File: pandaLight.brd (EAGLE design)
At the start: 100 x 50 mm, 163 parts, among them J1 PJ-037A, U1 MIC23450AAAYML, U10 51, U11 TPD12S016PWR, U12 N25Q128AF8, U13 TPD12S016PWR, U14 AS4C128M16D3, U15 PMOD-2X6, U16 PMOD-2X6, U17 PLR135-T10, U18 PLT133-T10W, U19 PLR135-T10, U2 6SLX45CSG324, U20 TP10SQ, U21 TP10SQ, U22 PAN1322, U3 TPD4S014SON, U4 FT2232HL, U5 93LC46BT-I/OT, U6 51, U7 51, U8 TPD12S016PWR, U9 51, X1 USBUB-S, X2 HDMI_RECEPTICAL_A, X3 HDMI_RECEPTICAL_A, X4 HDMI_RECEPTICAL_A, Y1 403, Y2 20Mhz

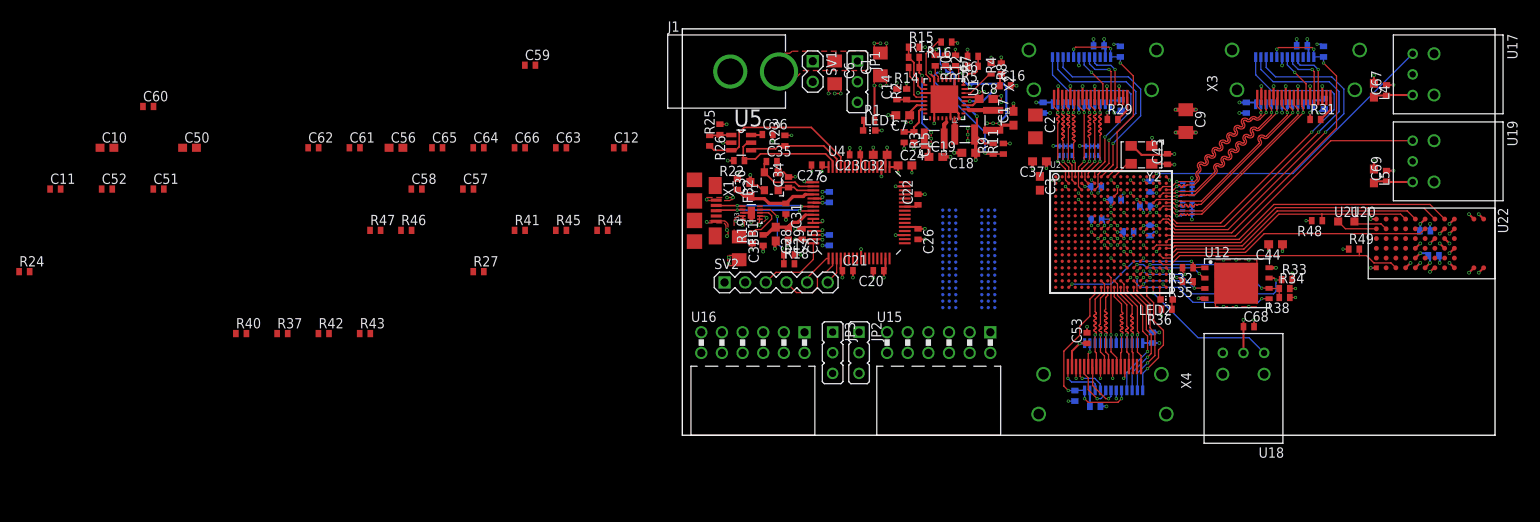
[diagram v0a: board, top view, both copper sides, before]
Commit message: Moved the pullup resistor networks and removed vias from the HDMI_RX* traces
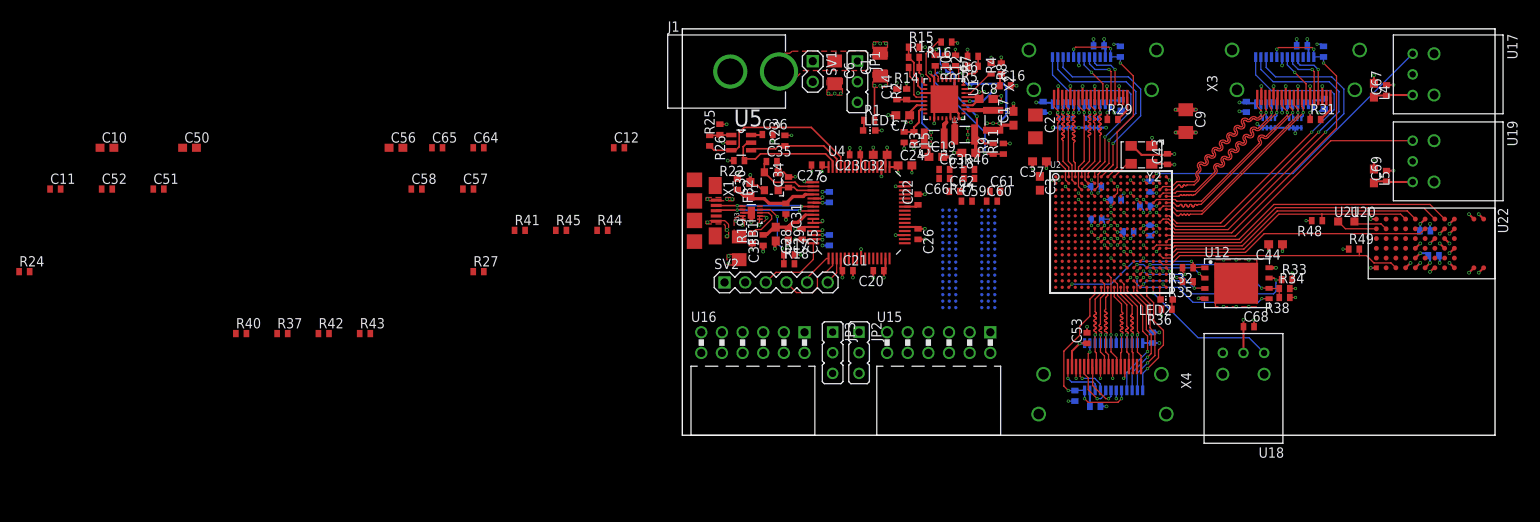
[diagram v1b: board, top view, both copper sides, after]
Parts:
- moved C60 104.5 mm to (38.1, 28.8)
- moved C62 79.1 mm to (33.5, 30.0)
- moved C61 79.0 mm to (38.5, 30.0)
- moved R47 73.3 mm to (35.3, 31.6), turned to 180 degrees
- moved R46 69.7 mm to (35.3, 32.7)
- moved C59 56.3 mm to (35.0, 28.8)
- moved C66 52.4 mm to (32.2, 31.6), turned to 180 degrees
- moved C63 47.2 mm to (32.2, 32.7)
- moved U10 16.9 mm to (75.4, 38.4), turned to 180 degrees
- moved U9 12.9 mm to (72.2, 38.4), turned to 180 degrees
- moved U6 3.40 mm to (47.2, 38.4), turned to 180 degrees
- moved U7 3.40 mm to (50.4, 38.4), turned to 180 degrees
- moved C42 0.10 mm to (44.4, 40.4)
- moved C49 0.10 mm to (69.4, 40.4)
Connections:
- net HDMI_RX0_CLK_N: now also U7.4; no longer U7.1
- net HDMI_RX0_CLK_P: now also U7.3; no longer U7.2
- net HDMI_RX0_DATA0_N: now also U7.2; no longer U7.3
- net HDMI_RX0_DATA0_P: now also U7.1; no longer U7.4
- net HDMI_RX0_DATA1_N: now also U6.4; no longer U6.1
- net HDMI_RX0_DATA1_P: now also U6.3; no longer U6.2
- net HDMI_RX0_DATA2_N: now also U6.2; no longer U6.3
- net HDMI_RX0_DATA2_P: now also U6.1; no longer U6.4
- net HDMI_RX1_CLK_N: now also U10.4; no longer U10.1
- net HDMI_RX1_CLK_P: now also U10.3; no longer U10.2
- net HDMI_RX1_DATA0_N: now also U10.2; no longer U10.3
- net HDMI_RX1_DATA0_P: now also U10.1; no longer U10.4
- net HDMI_RX1_DATA1_N: now also U9.4; no longer U9.1
- net HDMI_RX1_DATA1_P: now also U9.3; no longer U9.2
- net HDMI_RX1_DATA2_N: now also U9.2; no longer U9.3
- net HDMI_RX1_DATA2_P: now also U9.1; no longer U9.4
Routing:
- net +3V3: track 101.4 -> 105.6 mm, vias 72 -> 73
- net HDMI_RX1_CLK_N: track 26.4 -> 26.5 mm, vias 2 -> 1
- net HDMI_RX1_DATA1_N: vias 2 -> 1
- net HDMI_RX1_DATA2_P: track 24.6 -> 24.7 mm, vias 2 -> 1
- net HDMI_RX1_DATA0_P: track 25.9 -> 26.0 mm, vias 2 -> 1
- net HDMI_RX1_CLK_P: track 26.4 -> 26.5 mm, vias 2 -> 1
- net HDMI_RX1_DATA2_N: vias 2 -> 1
- net HDMI_RX1_DATA0_N: vias 2 -> 1
- net HDMI_RX1_DATA1_P: vias 2 -> 1
- net HDMI_RX0_DATA2_P: vias 2 -> 1
- net HDMI_RX0_DATA2_N: vias 2 -> 1
- net HDMI_RX0_DATA1_P: vias 2 -> 1
- net HDMI_RX0_DATA1_N: vias 2 -> 1
- net HDMI_RX0_DATA0_N: vias 2 -> 1
- net HDMI_RX0_CLK_P: vias 2 -> 1
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
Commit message: Began routing the DDR3 RAM
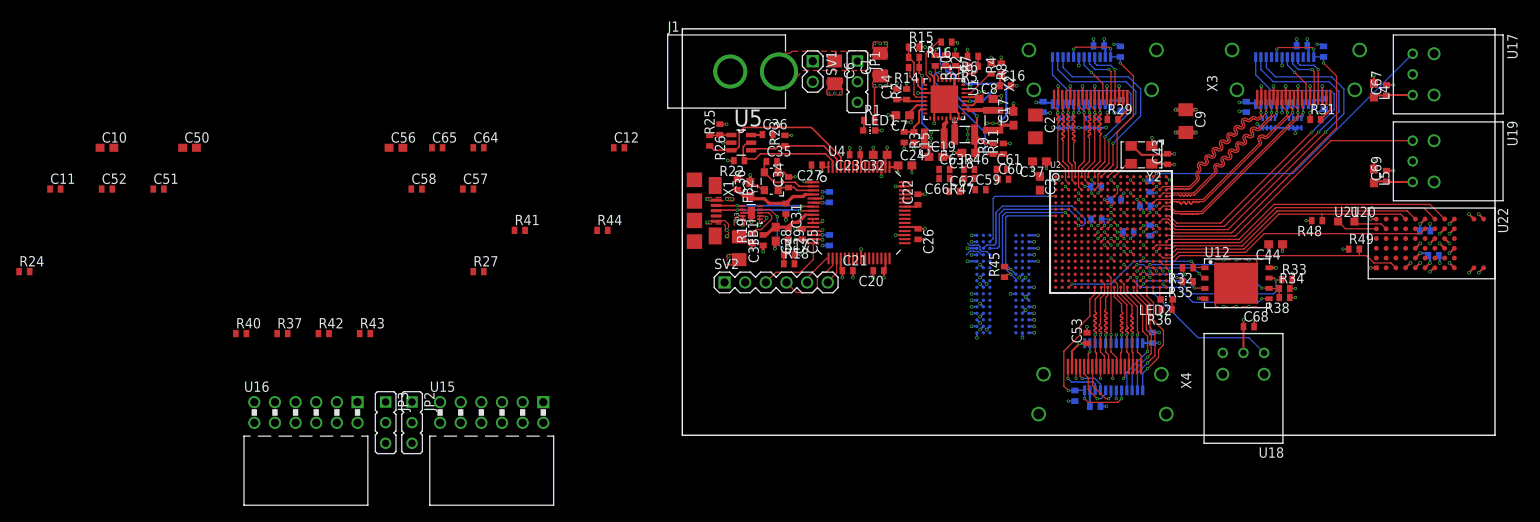
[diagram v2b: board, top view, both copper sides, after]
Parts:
- moved JP2 55.7 mm to (-33.2, 1.55)
- moved JP3 55.7 mm to (-36.5, 1.55)
- moved U15 55.7 mm to (-23.4, 2.80)
- moved U16 55.7 mm to (-46.3, 2.80)
- moved R45 54.8 mm to (39.6, 20.1), turned to 90 degrees
- moved U14 5.22 mm to (39.5, 18.6)
- moved C60 3.04 mm to (39.5, 31.5)
- moved C61 2.82 mm to (39.3, 32.7)
- moved C59 2.20 mm to (36.7, 30.2)
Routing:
- net DDR3_A5: track 0.00 -> 19.6 mm, vias 0 -> 1
- net DDR3_CK: track 0.00 -> 18.1 mm, vias 0 -> 2
- net DDR3_A2: track 0.00 -> 16.3 mm, vias 0 -> 1
- net GND: track 157.0 -> 172.9 mm, vias 160 -> 179
- net DDR3_CK#: track 0.00 -> 14.7 mm, vias 0 -> 2
- net DDR3_A9: track 0.00 -> 13.3 mm, vias 0 -> 1
- net +1V5: track 21.0 -> 32.1 mm, vias 7 -> 25
- net DDR3_A0: track 0.00 -> 3.63 mm
- net DDR3_A3: track 0.00 -> 2.47 mm

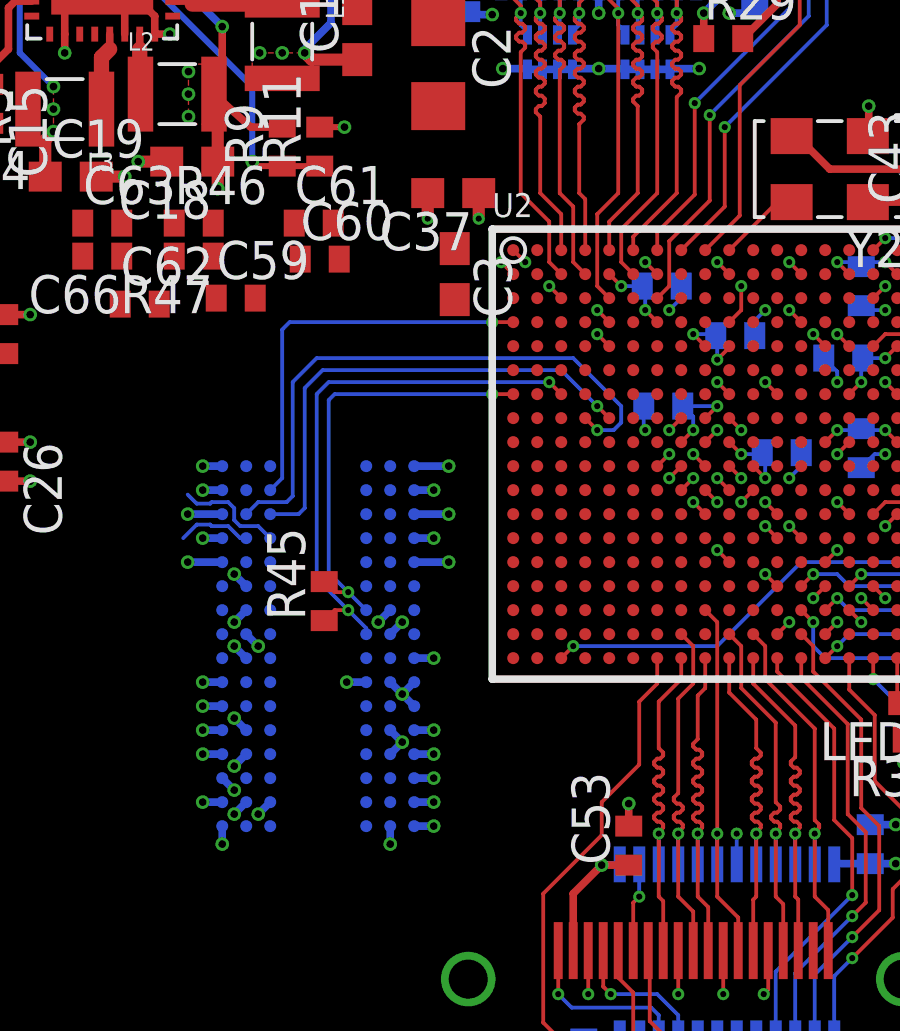
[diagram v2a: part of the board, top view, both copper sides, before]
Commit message: First routing of the DDR3 address lines
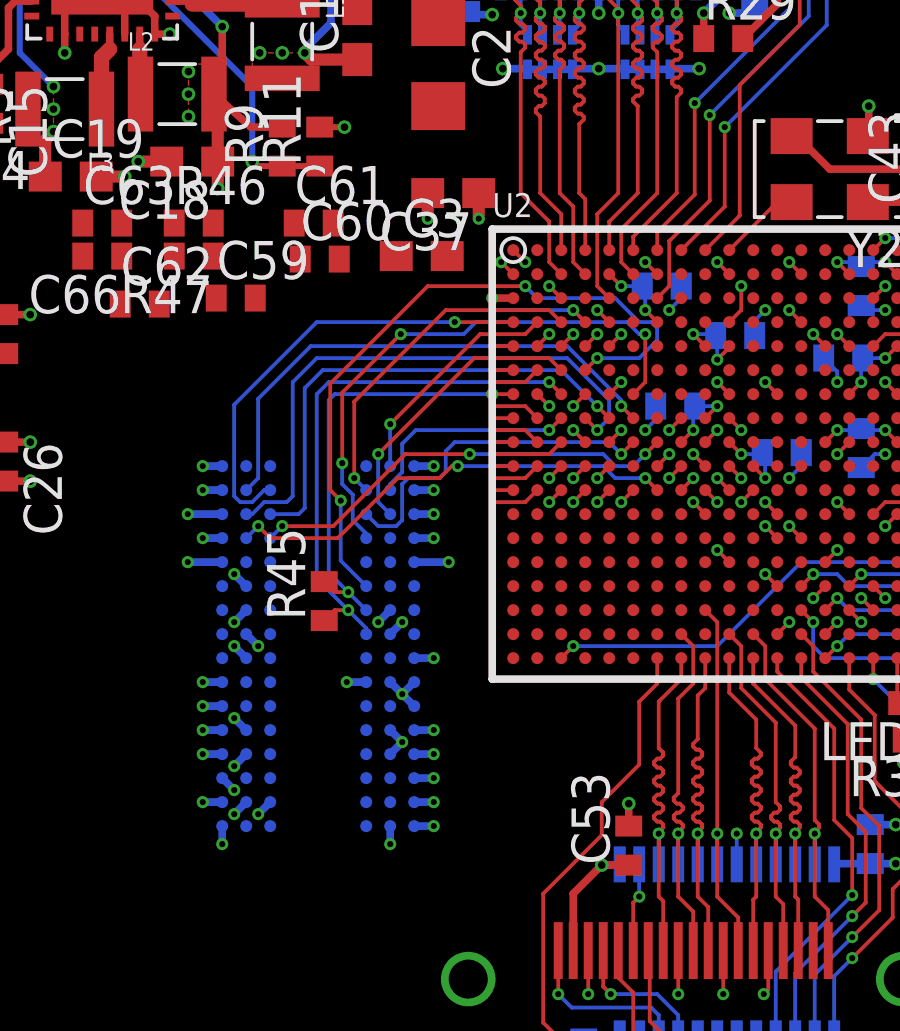
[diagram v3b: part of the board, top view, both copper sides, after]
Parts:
- moved C3 1.25 mm to (42.9, 31.6), turned to 0 degrees
- moved C5 0.40 mm to (51.4, 26.6)
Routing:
- net DDR3_A10: track 0.00 -> 23.3 mm, vias 0 -> 3
- net DDR3_A12: track 0.00 -> 18.6 mm, vias 0 -> 3
- net DDR3_A7: track 0.00 -> 17.6 mm, vias 0 -> 1
- net DDR3_A3: track 2.47 -> 15.4 mm, vias 0 -> 3
- net DDR3_A1: track 0.00 -> 11.7 mm, vias 0 -> 1
- net DDR3_A11: track 0.00 -> 11.4 mm, vias 0 -> 1
- net DDR3_A0: track 3.63 -> 14.6 mm, vias 0 -> 3
- net DDR3_A4: track 0.00 -> 9.76 mm, vias 0 -> 1
- net DDR3_A8: track 0.00 -> 7.71 mm, vias 0 -> 1
- net DDR3_A6: track 0.00 -> 7.37 mm, vias 0 -> 1
- net +1V5: track 32.1 -> 35.5 mm, vias 25 -> 28
- net N$35: track 0.00 -> 3.27 mm, vias 0 -> 1
- net DDR3_DQ6: track 0.00 -> 2.47 mm
- net DDR3_DQ4: track 0.00 -> 1.67 mm
- net DDR3_DQ2: track 0.00 -> 1.67 mm
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
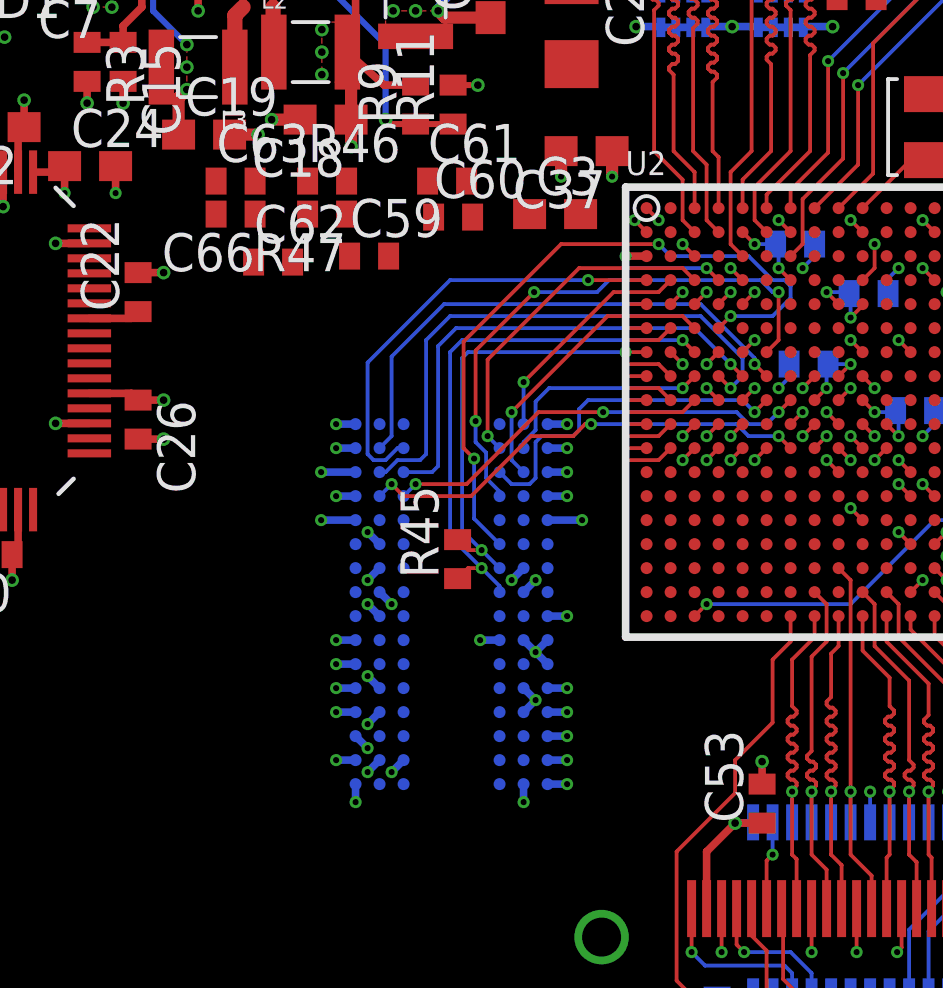
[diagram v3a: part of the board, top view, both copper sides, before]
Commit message: Finished routing the first DDR3 signal group: A* BA* RAS# CAS# WE#, now to length matching that group...
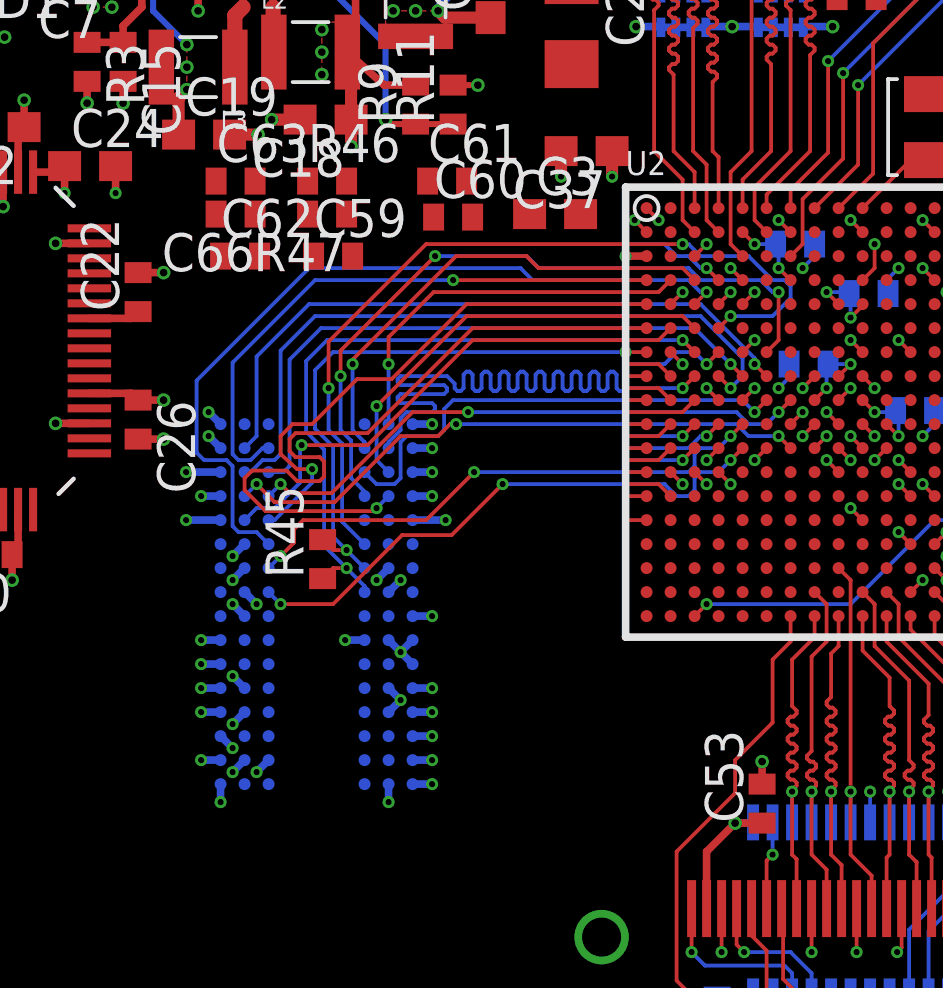
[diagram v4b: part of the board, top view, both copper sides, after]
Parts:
- moved R45 4.50 mm to (35.1, 20.1)
- moved U14 4.50 mm to (35.0, 18.6)
- moved C59 1.20 mm to (35.5, 30.2)
- moved C62 1.12 mm to (32.4, 30.2)
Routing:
- net DDR3_WE#: track 0.57 -> 26.7 mm
- net DDR3_BA1: track 0.70 -> 24.3 mm, vias 0 -> 1
- net DDR3_A6: track 7.37 -> 27.7 mm
- net DDR3_RAS#: track 0.57 -> 18.7 mm, vias 1 -> 3
- net DDR3_CAS#: track 0.57 -> 18.3 mm, vias 1 -> 3
- net DDR3_BA2: track 0.70 -> 18.3 mm, vias 0 -> 1
- net DDR3_BA0: track 1.67 -> 17.6 mm, vias 0 -> 1
- net DDR3_A8: track 7.71 -> 13.1 mm
- net DDR3_A12: track 18.6 -> 23.7 mm
- net DDR3_CK#: track 14.7 -> 19.5 mm
- net DDR3_A11: track 11.4 -> 16.3 mm
- net DDR3_A0: track 14.6 -> 19.3 mm
- net DDR3_CK: track 18.1 -> 22.9 mm
- net DDR3_A3: track 15.4 -> 20.0 mm
- net DDR3_A4: track 9.76 -> 14.4 mm
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
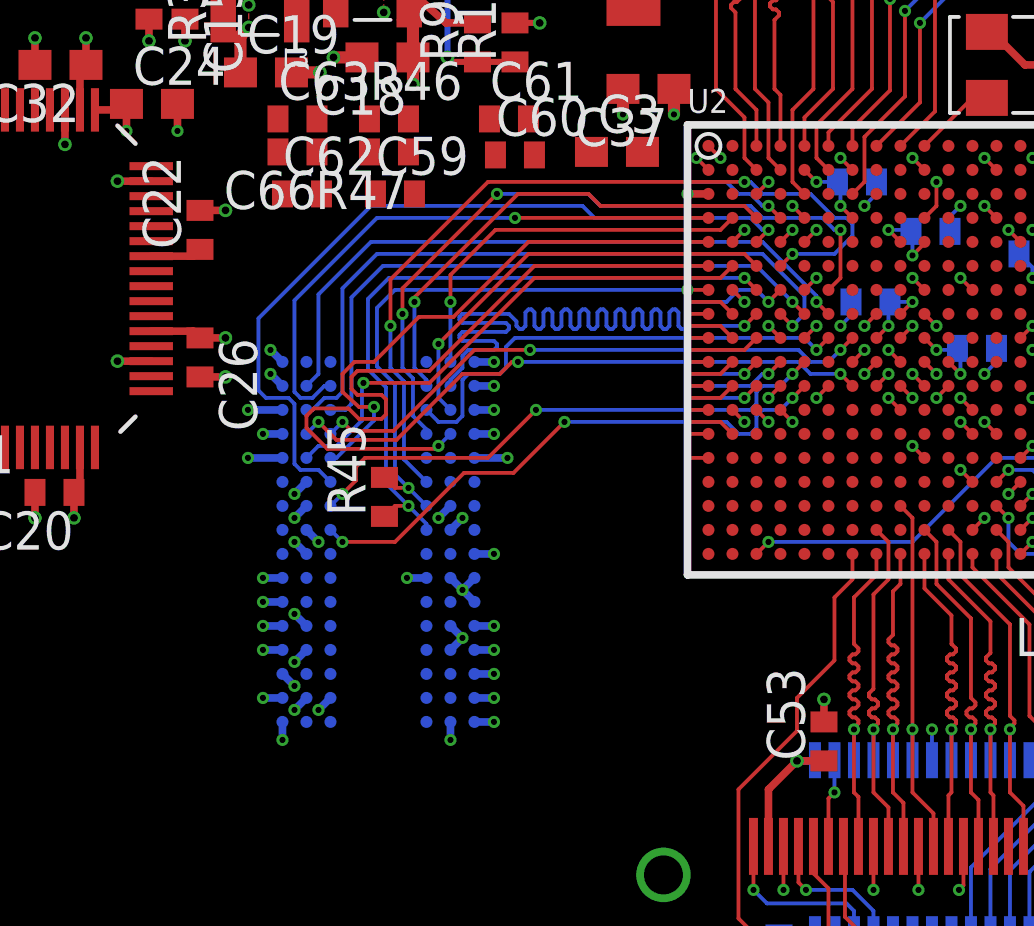
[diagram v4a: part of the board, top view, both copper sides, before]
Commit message: Some tweaking and length matching of the DDR3 traces
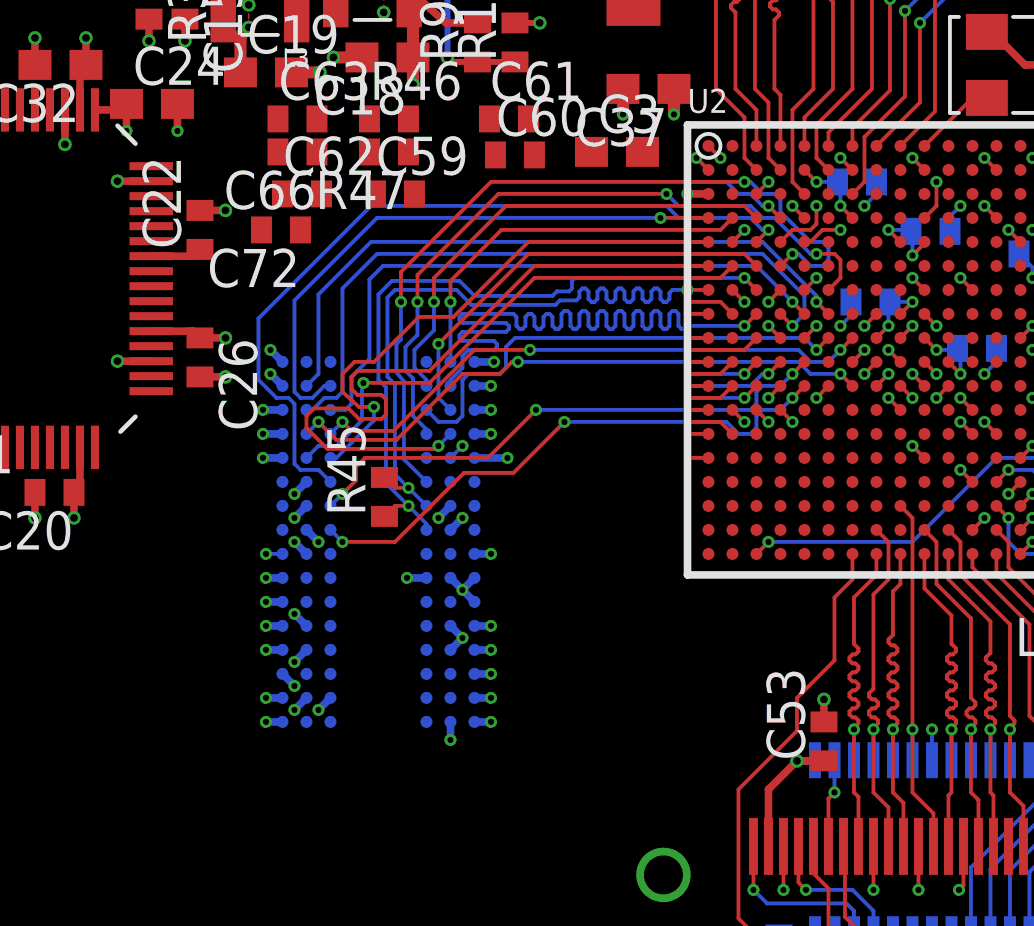
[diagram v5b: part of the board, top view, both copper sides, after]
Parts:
- added C72: 0.1u, pandaLight:0402
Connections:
- net +1V5_VREF: now also C72.1
- net GND: now also C72.2
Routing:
- net +1V5: track 39.0 -> 33.6 mm
- net DDR3_CK#: track 19.5 -> 23.1 mm
- net GND: track 174.2 -> 172.5 mm
- net DDR3_RESET#: track 0.57 -> 2.05 mm
- net DDR3_A10: track 27.8 -> 26.5 mm
- net DDR3_A6: track 27.7 -> 26.5 mm
- net +1V5_VREF: track 0.70 -> 1.82 mm, vias 1 -> 3
- net +3V3: track 105.6 -> 106.4 mm
- net DDR3_A12: track 23.7 -> 23.1 mm
